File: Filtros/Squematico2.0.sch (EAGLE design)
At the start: 8 parts, among them IC1 LM358N, M1 ELECTRET_MICROPHON-WM-62PC/62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

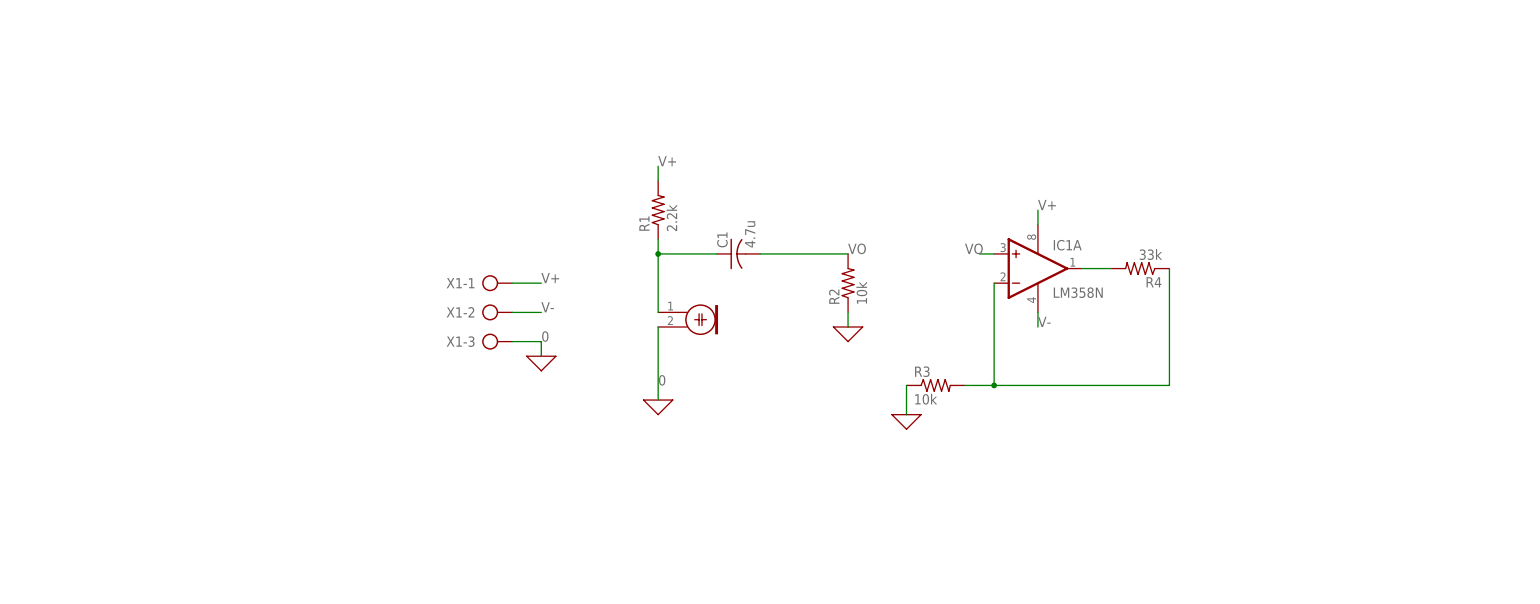
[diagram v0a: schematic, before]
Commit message: Se agregan pistas para los filtros y se crean los comparadores
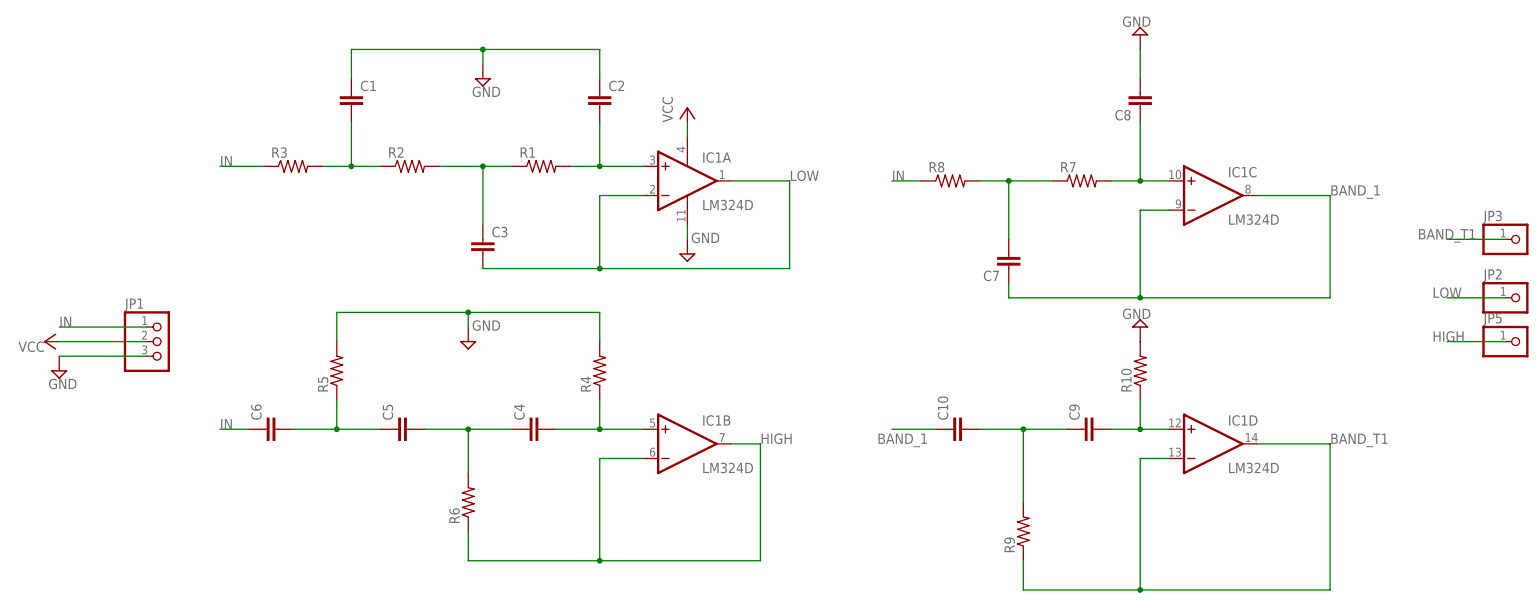
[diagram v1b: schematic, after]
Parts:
- removed M1: ELECTRET_MICROPHON-WM-62PC/62PK, microphon:ELECTRET_MICROPHON-WM-62PC/62PK
- removed X1: (no value), con-ptr500:AK300/3
- added C10, C2, C3, C4, C5, C6, C7, C8, C9: (no value), rcl:C-EU025-025X050
- added JP1: (no value), pinhead:PINHD-1X3
- added JP2, JP3, JP5: (no value), pinhead:PINHD-1X1
- added R10, R5, R6, R7, R8, R9: (no value), rcl:R-US_0204/7
- C1: value 4.7u -> (none); device rcl:C-US025-024X044 -> rcl:C-EU025-025X050
- IC1: value LM358N -> LM324D; device linear:LM358N -> linear:LM324D
- R1: value 2.2k -> (none); device rcl:R-US_0207/10 -> rcl:R-US_0204/7
- R2, R3: value 10k -> (none); device rcl:R-US_0207/10 -> rcl:R-US_0204/7
- R4: value 33k -> (none); device rcl:R-US_0207/10 -> rcl:R-US_0204/7
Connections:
- removed net 0: M1.2, R2.1, R3.1, X1-3.KL
- removed net N$5: IC1A.OUT, R4.2
- removed net V+: IC1P.V+, R1.2, X1-1.KL
- removed net V-: IC1P.V-, X1-2.KL
- removed net VO: C1.2, IC1A.+IN, R2.2
- new net BAND_1: C10.1, C7.1, IC1C.-IN, IC1C.OUT
- new net BAND_T1: IC1D.-IN, IC1D.OUT, JP3.1, R9.1
- new net GND: C1.1, C2.1, C8.2, IC1P.V-, JP1.3, R10.2, R4.2, R5.2
- new net HIGH: IC1B.-IN, IC1B.OUT, JP5.1, R6.1
- new net IN: C6.1, JP1.1, R3.1, R8.1
- new net LOW: C3.2, IC1A.-IN, IC1A.OUT, JP2.1
- new net N$11: C9.2, IC1D.+IN, R10.1
- new net N$14: C10.2, C9.1, R9.2
- new net N$2: C3.1, R1.1, R2.2
- new net N$3: C1.2, R2.1, R3.2
- new net N$6: C4.1, C5.2, R6.2
- new net N$7: C5.1, C6.2, R5.1
- new net N$8: C7.2, R7.1, R8.2
- new net N$9: C8.1, IC1C.+IN, R7.2
- new net VCC: IC1P.V+, JP1.2
- net N$1: now also C2.2, IC1A.+IN, R1.2; no longer C1.1, M1.1, R1.1
- net N$4: now also C4.2, IC1B.+IN; no longer IC1A.-IN, R3.2
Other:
- moved on the sheet: C1, IC1A, R1, R2, R3, R4
